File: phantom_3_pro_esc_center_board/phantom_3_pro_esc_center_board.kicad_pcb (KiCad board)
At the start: 2 copper layers, 123 x 123 mm, 351 parts

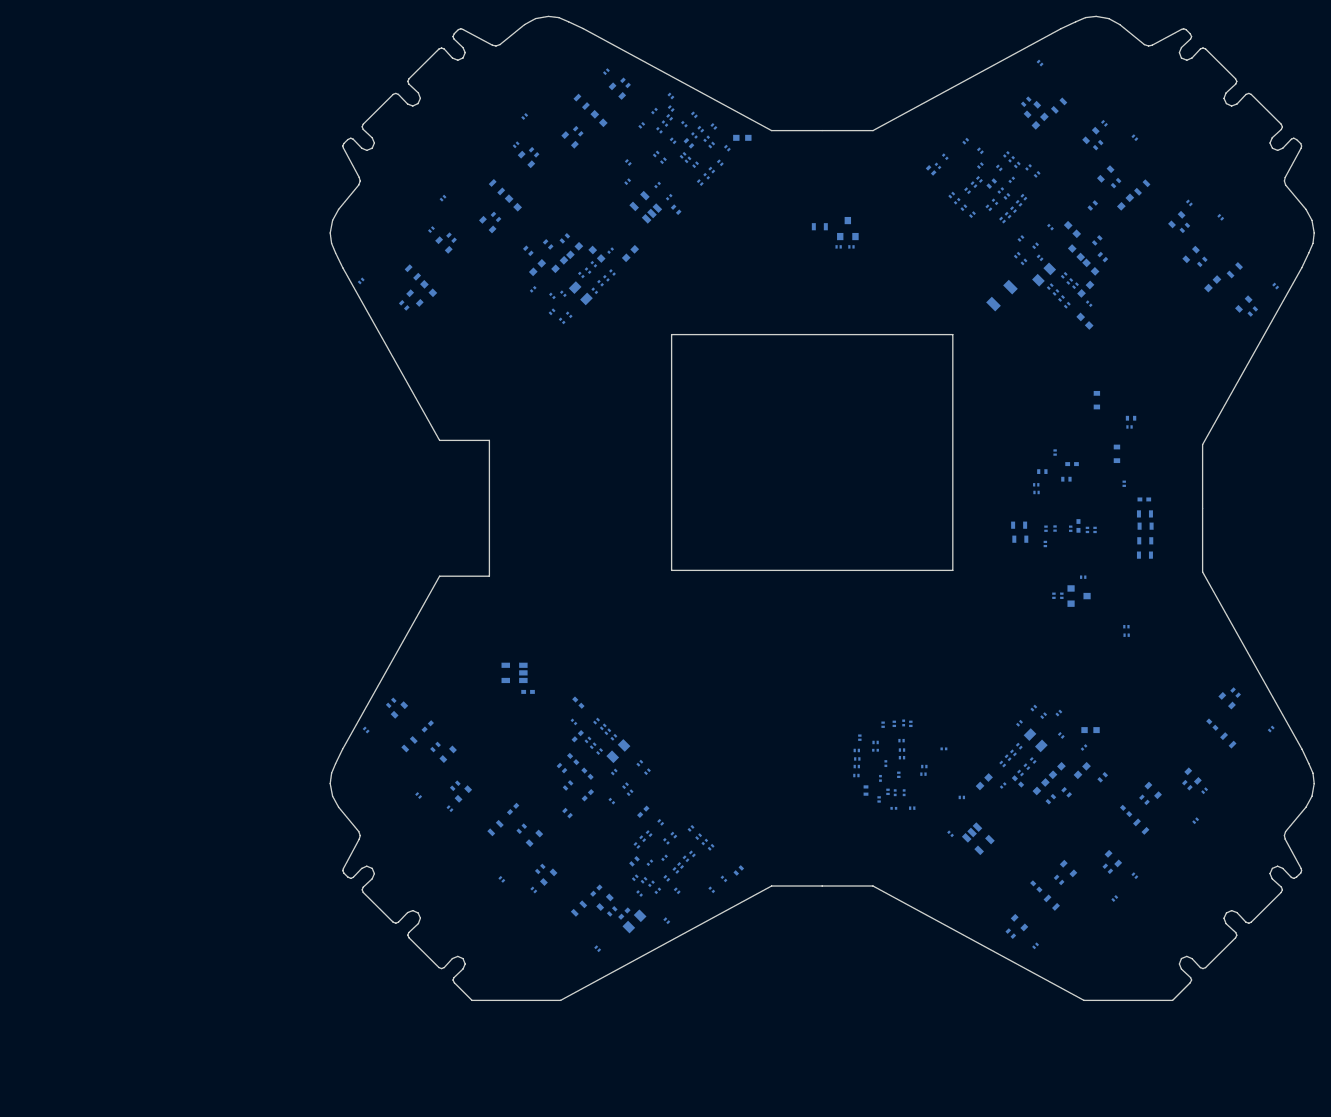
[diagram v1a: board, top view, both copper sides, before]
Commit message: ESC Center: Formed a link between schematic and PCB.
Modified PCB to link some components to schematic.

Also created edge pad connectors to FC board.
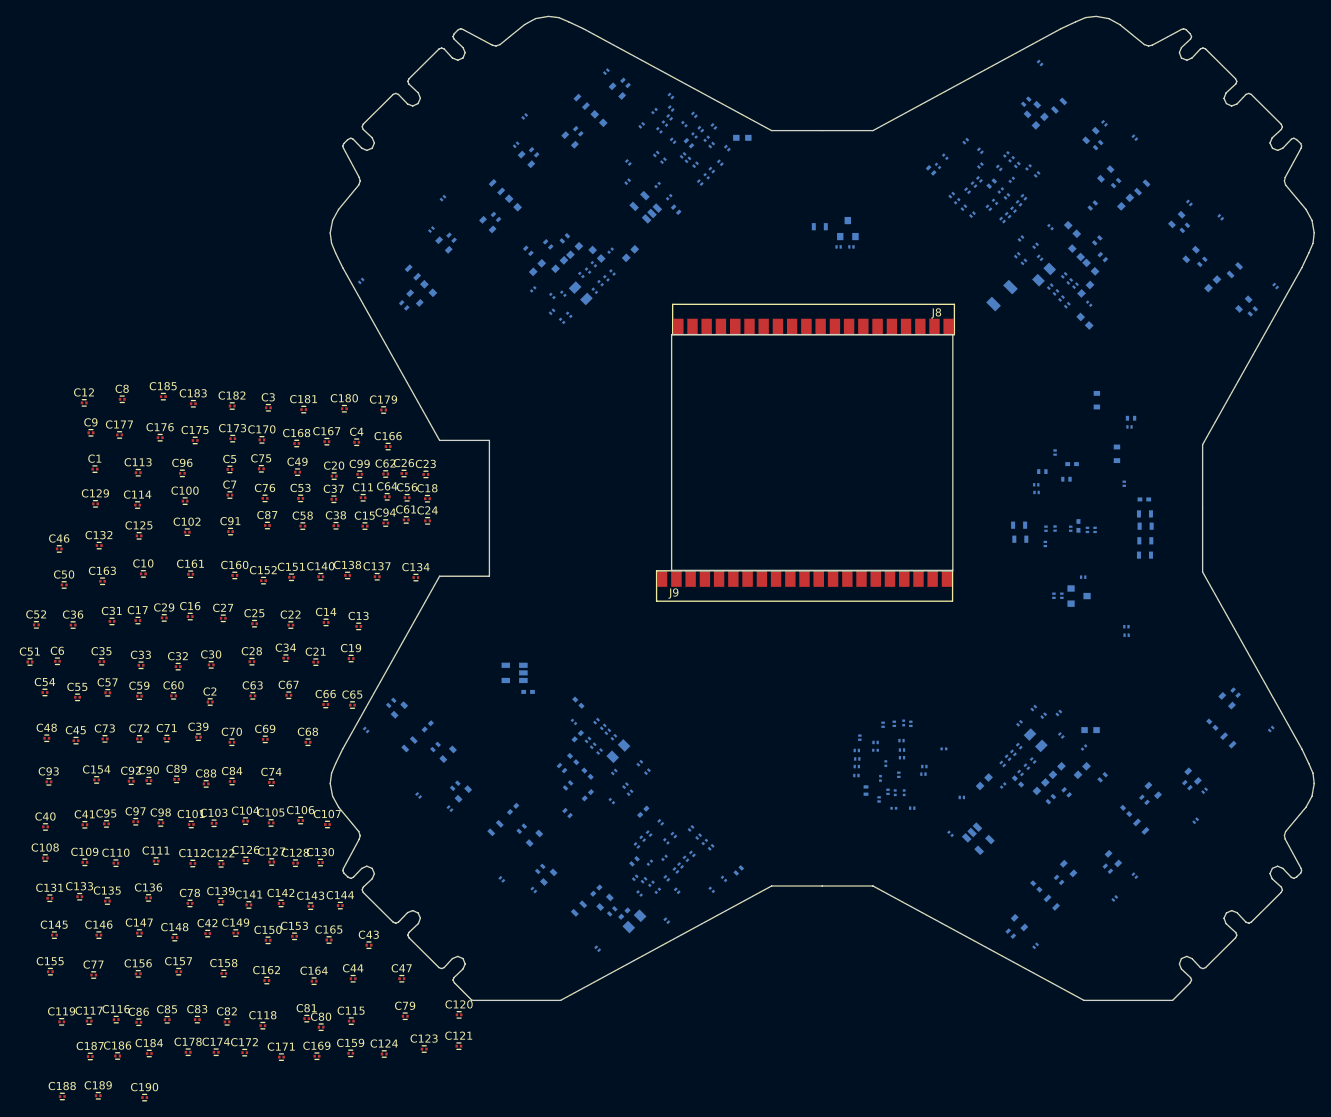
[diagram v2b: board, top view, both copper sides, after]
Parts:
- added C1: 100nF, Capacitors_SMD:C_0201, F.Cu at (60.9, 86.7)
- added C10: 100nF, Capacitors_SMD:C_0201, F.Cu at (66.9, 99.8)
- added C100: 1uF, Capacitors_SMD:C_0201, F.Cu at (72.1, 90.7)
- added C101: 2,2uF, Capacitors_SMD:C_0201, F.Cu at (72.9, 131.1)
- added C102: 1uF, Capacitors_SMD:C_0201, F.Cu at (72.4, 94.6)
- added C103: 2,2nF, Capacitors_SMD:C_0201, F.Cu at (75.7, 130.9)
- added C104: 2,2nF, Capacitors_SMD:C_0201, F.Cu at (79.7, 130.7)
- added C105: 4,7uF, Capacitors_SMD:C_0201, F.Cu at (82.9, 130.9)
- added C106: 0,1uF, Capacitors_SMD:C_0201, F.Cu at (86.6, 130.6)
- added C107: 2,2uF, Capacitors_SMD:C_0201, F.Cu at (89.9, 131.1)
- added C108: 2,2uF, Capacitors_SMD:C_0201, F.Cu at (54.6, 135.3)
- added C109: 2,2uF, Capacitors_SMD:C_0201, F.Cu at (59.6, 135.8)
- added C11: 15nF, Capacitors_SMD:C_0201, F.Cu at (94.4, 90.3)
- added C110: 2,2uF, Capacitors_SMD:C_0201, F.Cu at (63.5, 135.9)
- added C111: 2,2uF, Capacitors_SMD:C_0201, F.Cu at (68.5, 135.7)
- added C112: 2,2uF, Capacitors_SMD:C_0201, F.Cu at (73.1, 136.0)
- added C113: 36pF, Capacitors_SMD:C_0201, F.Cu at (66.3, 87.1)
- added C114: 36pF, Capacitors_SMD:C_0201, F.Cu at (66.2, 91.2)
- added C115: 100nF, Capacitors_SMD:C_0201, F.Cu at (92.9, 155.7)
- added C116: 220uF, Capacitors_SMD:C_0201, F.Cu at (63.5, 155.5)
- added C117: 220uF, Capacitors_SMD:C_0201, F.Cu at (60.1, 155.7)
- added C118: 100nF, Capacitors_SMD:C_0201, F.Cu at (81.8, 156.2)
- added C119: 100nF, Capacitors_SMD:C_0201, F.Cu at (56.7, 155.8)
- added C12: 4,7uF, Capacitors_SMD:C_0201, F.Cu at (59.5, 78.4)
- added C120: 100nF, Capacitors_SMD:C_0201, F.Cu at (106.4, 154.9)
- added C121: 120pF, Capacitors_SMD:C_0201, F.Cu at (106.3, 158.8)
- added C122: 6,8nF, Capacitors_SMD:C_0201, F.Cu at (76.6, 136.0)
- added C123: 100nF, Capacitors_SMD:C_0201, F.Cu at (102.0, 159.2)
- added C124: 100nF, Capacitors_SMD:C_0201, F.Cu at (97.0, 159.8)
- added C125: 15nF, Capacitors_SMD:C_0201, F.Cu at (66.4, 95.0)
- added C126: 4,7uF, Capacitors_SMD:C_0201, F.Cu at (79.7, 135.6)
- added C127: 0,1uF, Capacitors_SMD:C_0201, F.Cu at (82.9, 135.8)
- added C128: 0,1uF, Capacitors_SMD:C_0201, F.Cu at (85.9, 135.9)
- added C129: 47uF, Capacitors_SMD:C_0201, F.Cu at (60.9, 91.0)
- added C13: 0,1uF, Capacitors_SMD:C_0201, F.Cu at (93.8, 106.3)
- added C130: 0,1uF, Capacitors_SMD:C_0201, F.Cu at (89.0, 135.9)
- added C131: 2,2uF, Capacitors_SMD:C_0201, F.Cu at (55.2, 140.3)
- added C132: 1nF, Capacitors_SMD:C_0201, F.Cu at (61.4, 96.2)
- added C133: 0,1uF, Capacitors_SMD:C_0201, F.Cu at (58.9, 140.1)
- added C134: 22nF, Capacitors_SMD:C_0201, F.Cu at (101.0, 100.2)
- added C135: 2,2uF, Capacitors_SMD:C_0201, F.Cu at (62.4, 140.7)
- added C136: 0,1uF, Capacitors_SMD:C_0201, F.Cu at (67.5, 140.3)
- added C137: 1nF, Capacitors_SMD:C_0201, F.Cu at (96.1, 100.1)
- added C138: 1uF, Capacitors_SMD:C_0201, F.Cu at (92.4, 100.0)
- added C139: 2,2uF, Capacitors_SMD:C_0201, F.Cu at (76.6, 140.7)
- added C14: 0,1uF, Capacitors_SMD:C_0201, F.Cu at (89.7, 105.8)
- added C140: 1uF, Capacitors_SMD:C_0201, F.Cu at (89.1, 100.1)
- added C141: 2,2nF, Capacitors_SMD:C_0201, F.Cu at (80.1, 141.2)
- added C142: 2,2nF, Capacitors_SMD:C_0201, F.Cu at (84.1, 141.0)
- added C143: 4,7uF, Capacitors_SMD:C_0201, F.Cu at (87.8, 141.3)
- added C144: 0,1uF, Capacitors_SMD:C_0201, F.Cu at (91.5, 141.2)
- added C145: 2,2uF, Capacitors_SMD:C_0201, F.Cu at (55.8, 144.9)
- added C146: 2,2uF, Capacitors_SMD:C_0201, F.Cu at (61.3, 144.9)
- added C147: 2,2uF, Capacitors_SMD:C_0201, F.Cu at (66.4, 144.7)
- added C148: 2,2uF, Capacitors_SMD:C_0201, F.Cu at (70.8, 145.2)
- added C149: 2,2uF, Capacitors_SMD:C_0201, F.Cu at (78.5, 144.7)
- added C15: 47uF, Capacitors_SMD:C_0201, F.Cu at (94.6, 93.8)
- added C150: 2,2uF, Capacitors_SMD:C_0201, F.Cu at (82.5, 145.6)
- added C151: 36pF, Capacitors_SMD:C_0201, F.Cu at (85.4, 100.2)
- added C152: 36pF, Capacitors_SMD:C_0201, F.Cu at (81.9, 100.6)
- added C153: 4,7uF, Capacitors_SMD:C_0201, F.Cu at (85.8, 145.1)
- added C154: 4,7uF, Capacitors_SMD:C_0201, F.Cu at (61.1, 125.5)
- added C155: 2,2uF, Capacitors_SMD:C_0201, F.Cu at (55.3, 149.5)
- added C156: 4,7uF, Capacitors_SMD:C_0201, F.Cu at (66.3, 149.8)
- added C157: 4,7uF, Capacitors_SMD:C_0201, F.Cu at (71.3, 149.5)
- added C158: 2,2uF, Capacitors_SMD:C_0201, F.Cu at (77.0, 149.7)
- added C159: 270pF, Capacitors_SMD:C_0201, F.Cu at (92.8, 159.7)
- added C16: 0,1uF, Capacitors_SMD:C_0201, F.Cu at (72.8, 105.1)
- added C160: 10nF, Capacitors_SMD:C_0201, F.Cu at (78.3, 100.0)
- added C161: 10nF, Capacitors_SMD:C_0201, F.Cu at (72.8, 99.8)
- added C162: 2,2uF, Capacitors_SMD:C_0201, F.Cu at (82.3, 150.6)
- added C163: 10nF, Capacitors_SMD:C_0201, F.Cu at (61.8, 100.7)
- added C164: 2,2uF, Capacitors_SMD:C_0201, F.Cu at (88.2, 150.7)
- added C165: 3,3nF, Capacitors_SMD:C_0201, F.Cu at (90.1, 145.5)
- added C166: 10nF, Capacitors_SMD:C_0201, F.Cu at (97.5, 83.9)
- added C167: 10nF, Capacitors_SMD:C_0201, F.Cu at (89.8, 83.2)
- added C168: 1uF, Capacitors_SMD:C_0201, F.Cu at (86.1, 83.5)
- added C169: 100pF, Capacitors_SMD:C_0201, F.Cu at (88.6, 160.1)
- added C17: 2,2uF, Capacitors_SMD:C_0201, F.Cu at (66.2, 105.6)
- added C170: 1uF, Capacitors_SMD:C_0201, F.Cu at (81.7, 83.0)
- added C171: 100nF?, Capacitors_SMD:C_0201, F.Cu at (84.2, 160.2)
- added C172: 100nF, Capacitors_SMD:C_0201, F.Cu at (79.6, 159.6)
- added C173: 10nF, Capacitors_SMD:C_0201, F.Cu at (78.1, 82.9)
- added C174: 2,2nF?, Capacitors_SMD:C_0201, F.Cu at (76.0, 159.6)
- added C175: 47uF, Capacitors_SMD:C_0201, F.Cu at (73.4, 83.1)
- added C176: 47uF, Capacitors_SMD:C_0201, F.Cu at (69.0, 82.8)
- added C177: 10nF, Capacitors_SMD:C_0201, F.Cu at (63.9, 82.4)
- added C178: 22pF?, Capacitors_SMD:C_0201, F.Cu at (72.5, 159.6)
- added C179: 47uF, Capacitors_SMD:C_0201, F.Cu at (96.9, 79.3)
- added C18: 1nF, Capacitors_SMD:C_0201, F.Cu at (102.4, 90.4)
- added C180: 47uF, Capacitors_SMD:C_0201, F.Cu at (92.0, 79.1)
- added C181: 8uF, Capacitors_SMD:C_0201, F.Cu at (87.0, 79.2)
- added C182: 28uF, Capacitors_SMD:C_0201, F.Cu at (78.0, 78.8)
- added C183: 1uF, Capacitors_SMD:C_0201, F.Cu at (73.2, 78.5)
- added C184: 220pF, Capacitors_SMD:C_0201, F.Cu at (67.6, 159.7)
- added C185: ?pF, Capacitors_SMD:C_0201, F.Cu at (69.4, 77.6)
- added C186: 100uF, Capacitors_SMD:C_0201, F.Cu at (63.7, 160.0)
- added C187: 100uF, Capacitors_SMD:C_0201, F.Cu at (60.3, 160.1)
- added C188: 100uF, Capacitors_SMD:C_0201, F.Cu at (56.8, 165.1)
- added C189: 100uF, Capacitors_SMD:C_0201, F.Cu at (61.3, 165.0)
- added C19: 0,1uF, Capacitors_SMD:C_0201, F.Cu at (92.9, 110.4)
- added C190: 100uF, Capacitors_SMD:C_0201, F.Cu at (67.1, 165.2)
- added C2: 220uF, Capacitors_SMD:C_0201, F.Cu at (75.2, 115.8)
- added C20: 22nF, Capacitors_SMD:C_0201, F.Cu at (90.8, 87.5)
- added C21: 2,2uF, Capacitors_SMD:C_0201, F.Cu at (88.5, 110.8)
- added C22: 0,1uF, Capacitors_SMD:C_0201, F.Cu at (85.3, 106.2)
- added C23: 1nF, Capacitors_SMD:C_0201, F.Cu at (102.2, 87.3)
- added C24: 1uF, Capacitors_SMD:C_0201, F.Cu at (102.4, 93.2)
- added C25: 2,2uF, Capacitors_SMD:C_0201, F.Cu at (80.8, 106.0)
- added C26: 1uF, Capacitors_SMD:C_0201, F.Cu at (99.5, 87.2)
- added C27: 2,2nF, Capacitors_SMD:C_0201, F.Cu at (76.9, 105.3)
- added C28: 2,2nF, Capacitors_SMD:C_0201, F.Cu at (80.5, 110.8)
- added C29: 4,7uF, Capacitors_SMD:C_0201, F.Cu at (69.5, 105.3)
- added C3: 220uF, Capacitors_SMD:C_0201, F.Cu at (82.5, 79.0)
- added C30: 0,1uF, Capacitors_SMD:C_0201, F.Cu at (75.4, 111.2)
- added C31: 2,2uF, Capacitors_SMD:C_0201, F.Cu at (63.0, 105.7)
- added C32: 2,2uF, Capacitors_SMD:C_0201, F.Cu at (71.2, 111.4)
- added C33: 2,2uF, Capacitors_SMD:C_0201, F.Cu at (66.6, 111.2)
- added C34: 2,2uF, Capacitors_SMD:C_0201, F.Cu at (84.7, 110.3)
- added C35: 2,2uF, Capacitors_SMD:C_0201, F.Cu at (61.7, 110.8)
- added C36: 2,2uF, Capacitors_SMD:C_0201, F.Cu at (58.1, 106.2)
- added C37: 36pF, Capacitors_SMD:C_0201, F.Cu at (90.7, 90.5)
- added C38: 36pF, Capacitors_SMD:C_0201, F.Cu at (91.0, 93.8)
- added C39: 100nF, Capacitors_SMD:C_0201, F.Cu at (73.8, 120.2)
- added C4: 100nF, Capacitors_SMD:C_0201, F.Cu at (93.6, 83.3)
- added C40: 220uF, Capacitors_SMD:C_0201, F.Cu at (54.7, 131.4)
- added C41: 220uF, Capacitors_SMD:C_0201, F.Cu at (59.6, 131.1)
- added C42: 100nF, Capacitors_SMD:C_0201, F.Cu at (74.9, 144.7)
- added C43: 100nF, Capacitors_SMD:C_0201, F.Cu at (95.1, 146.2)
- added C44: 100nF, Capacitors_SMD:C_0201, F.Cu at (93.1, 150.4)
- added C45: 120pF, Capacitors_SMD:C_0201, F.Cu at (58.5, 120.6)
- added C46: 6,8nF, Capacitors_SMD:C_0201, F.Cu at (56.4, 96.7)
- added C47: 100nF, Capacitors_SMD:C_0201, F.Cu at (99.2, 150.4)
- added C48: 100nF, Capacitors_SMD:C_0201, F.Cu at (54.8, 120.3)
- added C49: 15nF, Capacitors_SMD:C_0201, F.Cu at (86.2, 87.1)
- added C5: 100nF, Capacitors_SMD:C_0201, F.Cu at (77.7, 86.7)
- added C50: 4,7uF, Capacitors_SMD:C_0201, F.Cu at (57.0, 101.2)
- added C51: 0,1uF, Capacitors_SMD:C_0201, F.Cu at (52.7, 110.8)
- added C52: 0,1uF, Capacitors_SMD:C_0201, F.Cu at (53.5, 106.2)
- added C53: 47uF, Capacitors_SMD:C_0201, F.Cu at (86.6, 90.3)
- added C54: 0,1uF, Capacitors_SMD:C_0201, F.Cu at (54.6, 114.6)
- added C55: 2,2uF, Capacitors_SMD:C_0201, F.Cu at (58.7, 115.2)
- added C56: 1nF, Capacitors_SMD:C_0201, F.Cu at (99.9, 90.3)
- added C57: 0,1uF, Capacitors_SMD:C_0201, F.Cu at (62.5, 114.6)
- added C58: 22nF, Capacitors_SMD:C_0201, F.Cu at (86.8, 93.8)
- added C59: 2,2uF, Capacitors_SMD:C_0201, F.Cu at (66.4, 115.1)
- added C6: 100nF, Capacitors_SMD:C_0201, F.Cu at (56.2, 110.7)
- added C60: 0,1uF, Capacitors_SMD:C_0201, F.Cu at (70.7, 115.0)
- added C61: 1nF, Capacitors_SMD:C_0201, F.Cu at (99.8, 93.0)
- added C62: 1uF, Capacitors_SMD:C_0201, F.Cu at (97.2, 87.3)
- added C63: 2,2uF, Capacitors_SMD:C_0201, F.Cu at (80.6, 115.0)
- added C64: 1uF, Capacitors_SMD:C_0201, F.Cu at (97.4, 90.1)
- added C65: 2,2nF, Capacitors_SMD:C_0201, F.Cu at (93.0, 116.2)
- added C66: 2,2nF, Capacitors_SMD:C_0201, F.Cu at (89.7, 116.1)
- added C67: 4,7uF, Capacitors_SMD:C_0201, F.Cu at (85.1, 115.0)
- added C68: 0,1uF, Capacitors_SMD:C_0201, F.Cu at (87.5, 120.8)
- added C69: 2,2uF, Capacitors_SMD:C_0201, F.Cu at (82.1, 120.5)
- added C7: 120pF, Capacitors_SMD:C_0201, F.Cu at (77.7, 89.9)
- added C70: 2,2uF, Capacitors_SMD:C_0201, F.Cu at (78.0, 120.8)
- added C71: 2,2uF, Capacitors_SMD:C_0201, F.Cu at (69.8, 120.4)
- added C72: 2,2uF, Capacitors_SMD:C_0201, F.Cu at (66.4, 120.4)
- added C73: 2,2uF, Capacitors_SMD:C_0201, F.Cu at (62.1, 120.4)
- added C74: 2,2uF, Capacitors_SMD:C_0201, F.Cu at (82.9, 125.8)
- added C75: 36pF, Capacitors_SMD:C_0201, F.Cu at (81.7, 86.6)
- added C76: 36pF, Capacitors_SMD:C_0201, F.Cu at (82.1, 90.3)
- added C77: 100nF, Capacitors_SMD:C_0201, F.Cu at (60.7, 149.9)
- added C78: 220uF, Capacitors_SMD:C_0201, F.Cu at (72.7, 141.0)
- added C79: 220uF, Capacitors_SMD:C_0201, F.Cu at (99.6, 155.1)
- added C8: 6,8nF, Capacitors_SMD:C_0201, F.Cu at (64.3, 78.0)
- added C80: 100nF, Capacitors_SMD:C_0201, F.Cu at (89.1, 156.4)
- added C81: 100nF, Capacitors_SMD:C_0201, F.Cu at (87.3, 155.4)
- added C82: 100nF, Capacitors_SMD:C_0201, F.Cu at (77.4, 155.8)
- added C83: 120pF, Capacitors_SMD:C_0201, F.Cu at (73.7, 155.5)
- added C84: 6,8nF, Capacitors_SMD:C_0201, F.Cu at (78.0, 125.7)
- added C85: 100nF, Capacitors_SMD:C_0201, F.Cu at (69.9, 155.5)
- added C86: 100nF, Capacitors_SMD:C_0201, F.Cu at (66.3, 155.8)
- added C87: 15nF, Capacitors_SMD:C_0201, F.Cu at (82.4, 93.7)
- added C88: 4,7uF, Capacitors_SMD:C_0201, F.Cu at (74.8, 126.0)
- added C89: 0,1uF, Capacitors_SMD:C_0201, F.Cu at (71.1, 125.5)
- added C9: 100nF, Capacitors_SMD:C_0201, F.Cu at (60.4, 82.1)
- added C90: 0,1uF, Capacitors_SMD:C_0201, F.Cu at (67.6, 125.6)
- added C91: 47uF, Capacitors_SMD:C_0201, F.Cu at (77.8, 94.5)
- added C92: 0,1uF, Capacitors_SMD:C_0201, F.Cu at (65.4, 125.7)
- added C93: 2,2uF, Capacitors_SMD:C_0201, F.Cu at (55.1, 125.8)
- added C94: 1nF, Capacitors_SMD:C_0201, F.Cu at (97.2, 93.4)
- added C95: 0,1uF, Capacitors_SMD:C_0201, F.Cu at (62.3, 131.0)
- added C96: 22nF, Capacitors_SMD:C_0201, F.Cu at (71.8, 87.2)
- added C97: 2,2uF, Capacitors_SMD:C_0201, F.Cu at (66.0, 130.8)
- added C98: 0,1uF, Capacitors_SMD:C_0201, F.Cu at (69.1, 130.9)
- added C99: 1nF, Capacitors_SMD:C_0201, F.Cu at (94.0, 87.3)
- added J8: CONN_MC_FRONT, Connectors_custom:Connector-edge-20pin-1.78mm, F.Cu at (167.6, 69.9)
- added J9: CONN_MC_BACK, Connectors_custom:Connector-edge-21pin-1.78mm, F.Cu at (131.8, 99.4)
